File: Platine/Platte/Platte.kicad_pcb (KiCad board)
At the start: 2 copper layers, 31.1 x 31.1 mm, 11 parts, among them J1 Conn_01x07_MountingPin, J2 Conn_01x04_Socket, J3 Conn_01x04_Socket

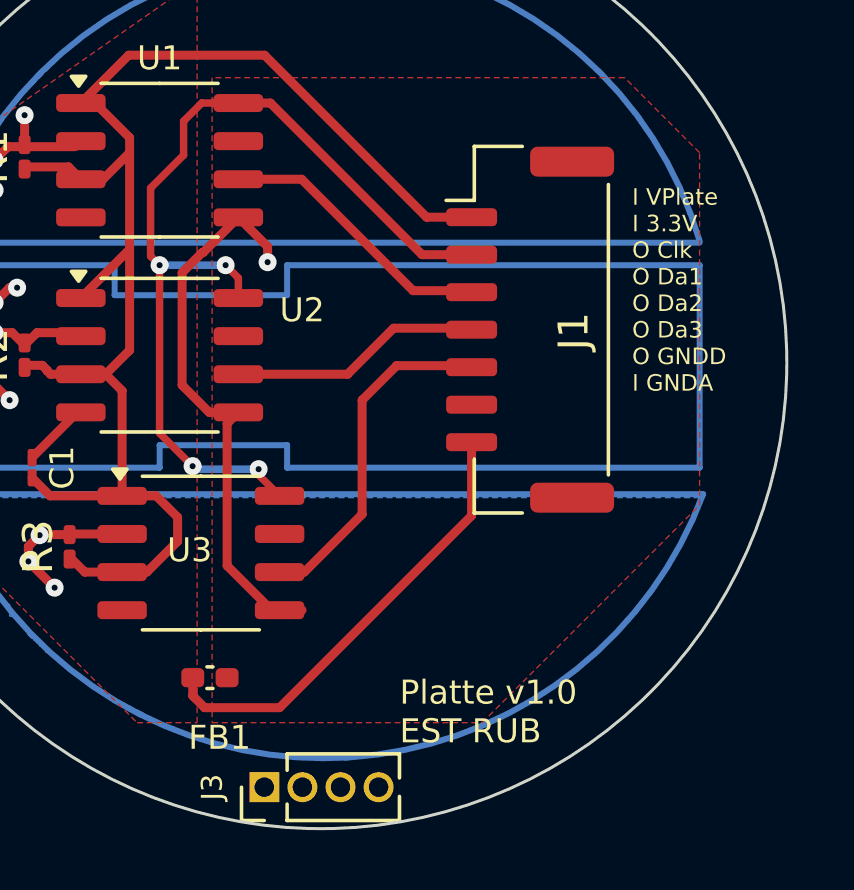
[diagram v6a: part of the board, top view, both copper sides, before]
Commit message: Mit Robin geredet, ein paar Veränderung gemacht
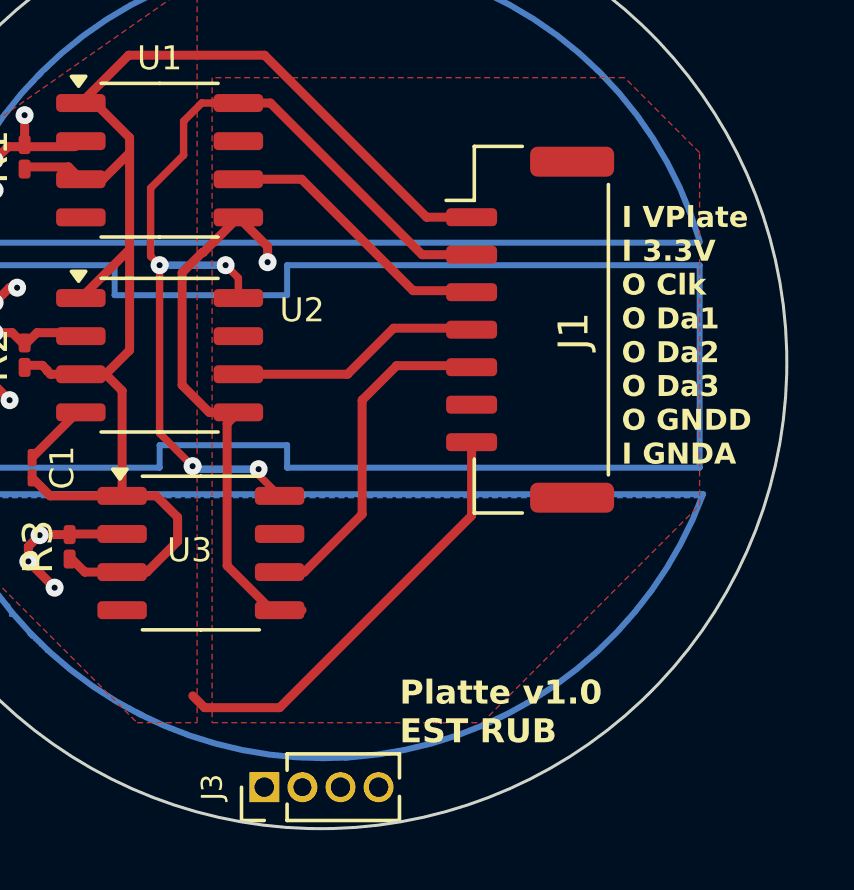
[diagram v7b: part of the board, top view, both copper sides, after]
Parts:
- removed FB1: FerriteBead, Inductor_SMD:L_0402_1005Metric_Pad0.77x0.64mm_HandSolder
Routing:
- net GNDA: track 17.6 -> 16.9 mm
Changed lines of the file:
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@@
 		)
 	)
-	(footprint "Inductor_SMD:L_0402_1005Metric_Pad0.77x0.64mm_HandSolder"
-		(layer "F.Cu")
-		(at 94.6775 80.25)
-		(descr "Inductor SMD 0402 (1005 Metric), square (rectangular) end terminal, IPC_7351 nominal with elongated pad for handsoldering. (Body size source: http://www.tortai-tech.com/upload/download/2011102023233369053.pdf), generated with kicad-footprint-generator")
-		(tags "inductor handsolder")
-		(property "Reference" "FB1"
-			(at 0.3225 2 0)
-			(layer "F.SilkS")
-			(effects
-				(font
-					(size 0.8 0.8)
-					(thickness 0.15)
-				)
-			)
-		)
-		(property "Value" "FerriteBead"
-			(at 0 1.17 0)
-			(layer "F.Fab")
-			(effects
-				(font
-					(size 1 1)
-					(thickness 0.15)
-				)
-			)
-		)
-		(property "Footprint" "Inductor_SMD:L_0402_1005Metric_Pad0.77x0.64mm_HandSolder"
-			(at 0 0 0)
-			(unlocked yes)
-			(layer "F.Fab")
-			(hide yes)
-			(effects
-				(font
-					(size 1.27 1.27)
-					(thickness 0.15)
-				)
-			)
-		)
-		(property "Datasheet" ""
-			(at 0 0 0)
-			(unlocked yes)
-			(layer "F.Fab")
-			(hide yes)
-			(effects
-				(font
-					(size 1.27 1.27)
-					(thickness 0.15)
-				)
-			)
-		)
-		(property "Description" "Ferrite bead"
-			(at 0 0 0)
-			(unlocked yes)
-			(layer "F.Fab")
-			(hide yes)
-			(effects
-				(font
-					(size 1.27 1.27)
-					(thickness 0.15)
-				)
-			)
-		)
-		(property ki_fp_filters "Inductor_* L_* *Ferrite*")
-		(sheetname "Stammblatt")
-		(sheetfile "Platte.kicad_sch")
-		(attr smd)
-		(fp_line
-			(start -0.1002 -0.36)
-			(end 0.1002 -0.36)
-			(stroke
-				(width 0.12)
-				(type solid)
-			)
-			(layer "F.SilkS")
-		)
-		(fp_line
-			(start -0.1002 0.36)
-			(end 0.1002 0.36)
-			(stroke
-				(width 0.12)
-				(type solid)
-			)
-			(layer "F.SilkS")
-		)
-		(fp_line
-			(start -1.1 -0.47)
-			(end 1.1 -0.47)
-			(stroke
-				(width 0.05)
-				(type solid)
-			)
-			(layer "F.CrtYd")
-		)
-		(fp_line
-			(start -1.1 0.47)
-			(end -1.1 -0.47)
-			(stroke
-				(width 0.05)
-				(type solid)
-			)
-			(layer "F.CrtYd")
-		)
-		(fp_line
-			(start 1.1 -0.47)
-			(end 1.1 0.47)
-			(stroke
-				(width 0.05)
-				(type solid)
-			)
-			(layer "F.CrtYd")
-		)
-		(fp_line
-			(start 1.1 0.47)
-			(end -1.1 0.47)
-			(stroke
-				(width 0.05)
-				(type solid)
-			)
-			(layer "F.CrtYd")
-		)
-		(fp_line
-			(start -0.5 -0.25)
-			(end 0.5 -0.25)
-			(stroke
-				(width 0.1)
-				(type solid)
-			)
-			(layer "F.Fab")
-		)
-		(fp_line
-			(start -0.5 0.25)
-			(end -0.5 -0.25)
-			(stroke
-				(width 0.1)
-				(type solid)
-			)
-			(layer "F.Fab")
-		)
-		(fp_line
-			(start 0.5 -0.25)
-			(end 0.5 0.25)
-			(stroke
-				(width 0.1)
-				(type solid)
-			)
-			(layer "F.Fab")
-		)
-		(fp_line
-			(start 0.5 0.25)
-			(end -0.5 0.25)
-			(stroke
-				(width 0.1)
-				(type solid)
-			)
-			(layer "F.Fab")
-		)
-		(fp_text user "${REFERENCE}"
-			(at 0 0 0)
-			(layer "F.Fab")
-			(effects
-				(font
-					(size 0.25 0.25)
-					(thickness 0.04)
-				)
-			)
-		)
-		(pad "1" smd roundrect
-			(at -0.5725 0)
-			(size 0.765 0.64)
-			(layers "F.Cu" "F.Paste" "F.Mask")
-			(roundrect_rratio 0.25)
-			(net 1 "GNDA")
-			(pintype "passive")
-		)
-		(pad "2" smd roundrect
-			(at 0.5725 0)
-			(size 0.765 0.64)
-			(layers "F.Cu" "F.Paste" "F.Mask")
-			(roundrect_rratio 0.25)
-			(net 2 "GNDD")
-			(pintype "passive")
-		)
-		(model "${KICAD8_3DMODEL_DIR}/Inductor_SMD.3dshapes/L_0402_1005Metric.wrl"
-			(offset
-				(xyz 0 0 0)
-			)
-			(scale
-				(xyz 1 1 1)
-			)
-			(rotate
-				(xyz 0 0 0)
-			)
-		)
-	)
 	(footprint "Resistor_SMD:R_0201_0603Metric_Pad0.64x0.40mm_HandSolder"
 		(layer "F.Cu")
@@
 			(at 0 1.27 90)
 			(size 1 1)
-			(drill 0.65)
+			(drill 0.6)
 			(layers "*.Cu" "*.Mask")
 			(remove_unused_layers no)
@@
 	)
 	(gr_text "I VPlate\nI 3.3V\nO Clk\nO Da1\nO Da2\nO Da3\nO GNDD\nI GNDA"
-		(at 108.75 70.75 0)
+		(at 108.4 73.2 0)
 		(layer "F.SilkS")
 		(effects
 			(font
-				(size 0.55 0.55)
-				(thickness 0.125)
+				(size 0.7 0.7)
+				(thickness 0.175)
+				(bold yes)
 			)
 			(justify left bottom)
@@
 			(font
 				(size 0.8 0.8)
-				(thickness 0.15)
+				(thickness 0.2)
+				(bold yes)
 			)
 			(justify left bottom)
@@
 	)
 	(segment
-		(start 94.105 80.25)
-		(end 94.105 80.855)
-		(width 0.3)
-		(layer "F.Cu")
-		(net 1)
-	)
-	(segment
 		(start 97 81.25)
 		(end 103.4 74.85)
@@
 	)
 	(segment
-		(start 94.105 80.25)
-		(end 94 80.25)
-		(width 0.3)
-		(layer "F.Cu")
-		(net 1)
-	)
-	(segment
 		(start 90.2575 71.405)
 		(end 88.75 72.9125)
@@
 		(priority 2)
 		(connect_pads
-			(clearance 0.5)
+			(clearance 0.3)
 		)
-		(min_thickness 0.25)
+		(min_thickness 0.2)
 		(filled_areas_thickness no)
 		(fill yes
@@
 		(priority 1)
 		(connect_pads
-			(clearance 0.5)
+			(clearance 0.3)
 		)
-		(min_thickness 0.25)
+		(min_thickness 0.2)
 		(filled_areas_thickness no)
 		(fill yes

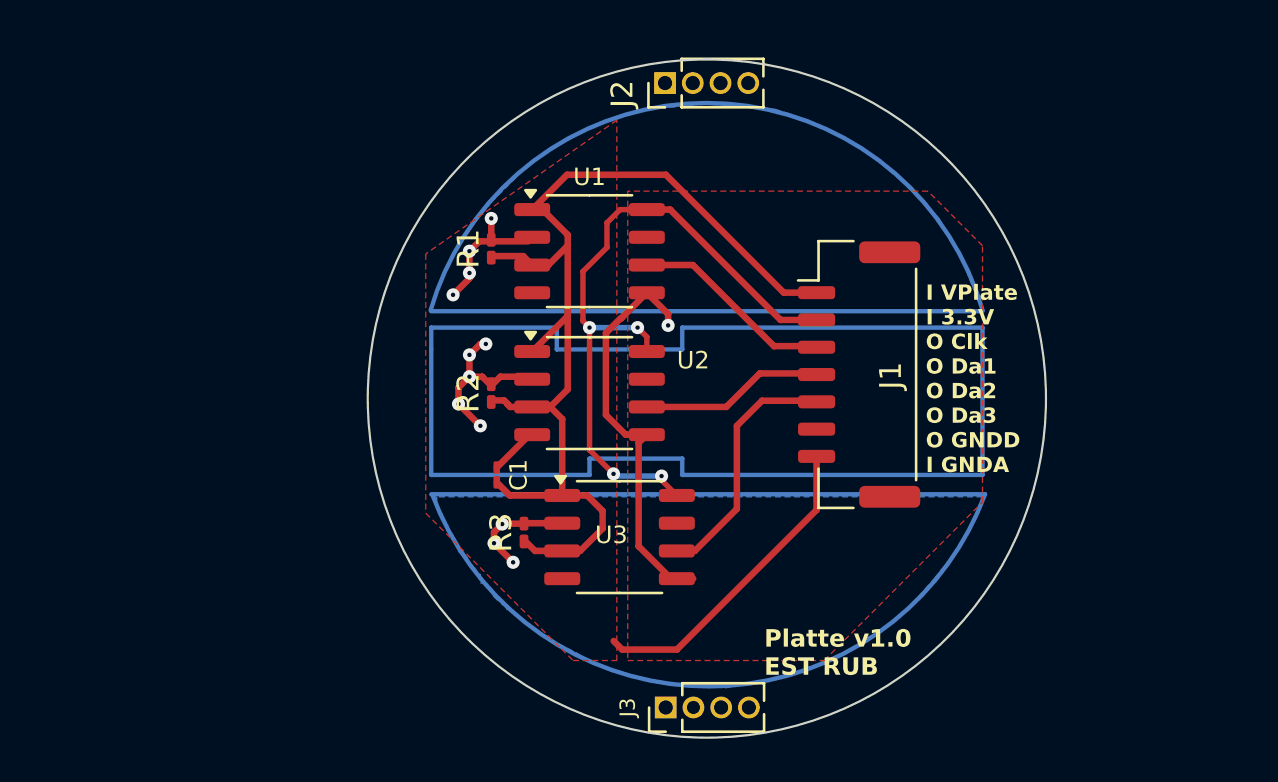
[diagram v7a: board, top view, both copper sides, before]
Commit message: LTSpice simulation done. Changing now schematics and PCB
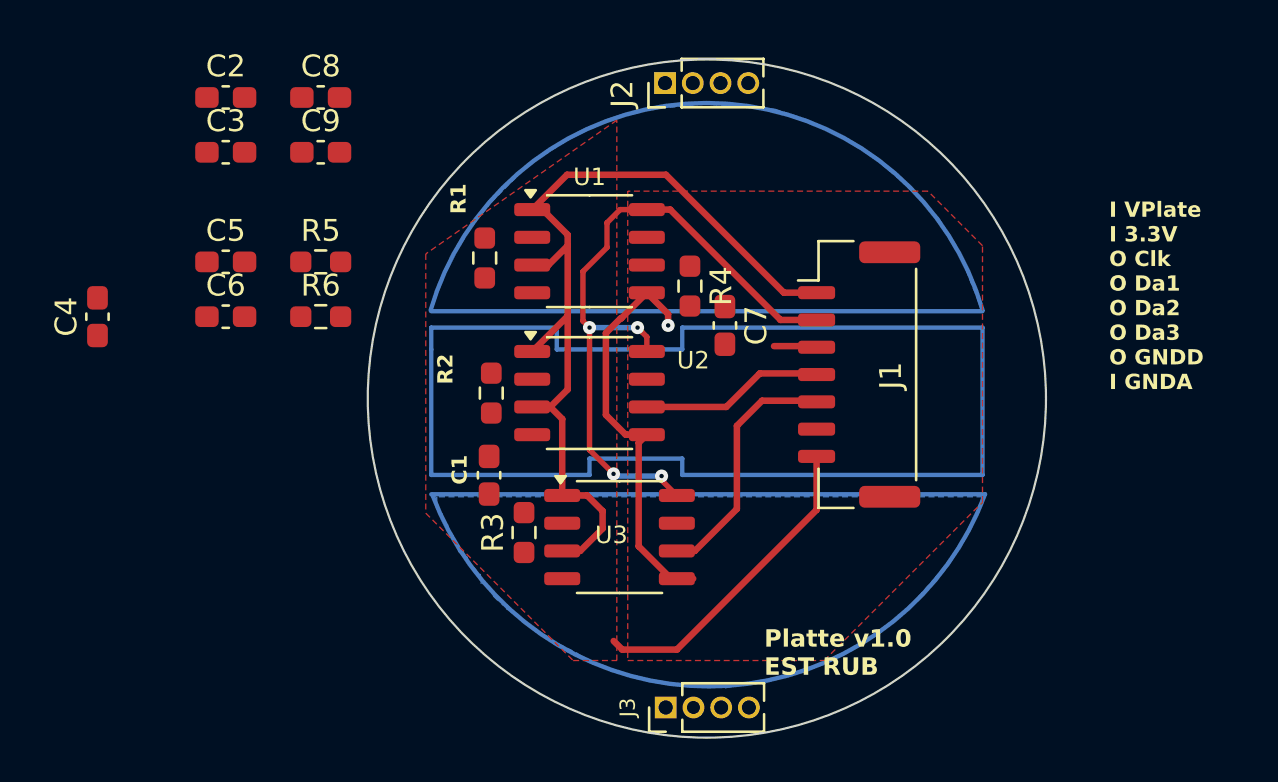
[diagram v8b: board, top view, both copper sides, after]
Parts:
- added C2: 0.1uF, Capacitor_SMD:C_0603_1608Metric_Pad1.08x0.95mm_HandSolder, F.Cu at (76.3, 56.0)
- added C3: 0.1uF, Capacitor_SMD:C_0603_1608Metric_Pad1.08x0.95mm_HandSolder, F.Cu at (76.3, 58.5)
- added C4: 0.1uF, Capacitor_SMD:C_0603_1608Metric_Pad1.08x0.95mm_HandSolder, F.Cu at (70.5, 66.0)
- added C5: 0.1uF, Capacitor_SMD:C_0603_1608Metric_Pad1.08x0.95mm_HandSolder, F.Cu at (76.3, 63.5)
- added C6: 0.1uF, Capacitor_SMD:C_0603_1608Metric_Pad1.08x0.95mm_HandSolder, F.Cu at (76.3, 66.0)
- added C7: 5n, Capacitor_SMD:C_0603_1608Metric_Pad1.08x0.95mm_HandSolder, F.Cu at (99.2, 66.4)
- added C8: 5n, Capacitor_SMD:C_0603_1608Metric_Pad1.08x0.95mm_HandSolder, F.Cu at (80.7, 56.0)
- added C9: 5n, Capacitor_SMD:C_0603_1608Metric_Pad1.08x0.95mm_HandSolder, F.Cu at (80.7, 58.5)
- added R4: 1k, Resistor_SMD:R_0603_1608Metric_Pad0.98x0.95mm_HandSolder, F.Cu at (97.6, 64.6)
- added R5: 1k, Resistor_SMD:R_0603_1608Metric_Pad0.98x0.95mm_HandSolder, F.Cu at (80.7, 63.5)
- added R6: 1k, Resistor_SMD:R_0603_1608Metric_Pad0.98x0.95mm_HandSolder, F.Cu at (80.7, 66.0)
- C1: footprint Capacitor_SMD:C_01005_0402Metric_Pad0.57x0.30mm_HandSolder -> Capacitor_SMD:C_0603_1608Metric_Pad1.08x0.95mm_HandSolder
- R1, R2, R3: value R -> 12.5; footprint Resistor_SMD:R_0201_0603Metric_Pad0.64x0.40mm_HandSolder -> Resistor_SMD:R_0603_1608Metric_Pad0.98x0.95mm_HandSolder
- moved R1 0.52 mm to (88.2, 63.3)
- moved C1 0.35 mm to (88.4, 73.3)
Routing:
- net +3.3VA: track 50.1 -> 40.9 mm
- net /analog_inp_2: track 8.09 -> 0.16 mm, vias 5 -> 0
- net /amp_data1: track 9.31 -> 1.95 mm
- net /analog_inp_1: track 6.17 -> 0.00 mm, vias 4 -> 0
- net /analog_inp_3: track 5.13 -> 0.00 mm, vias 3 -> 0
- net GNDA: track 16.9 -> 14.7 mm
